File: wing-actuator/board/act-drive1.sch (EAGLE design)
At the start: 137 parts, among them J1 POWER_JACKPTH_LOCK, Q1 BSS123, Q2 BSS123, Q3 BSS123, Q4 BSS123, Q5 BSS123, Q6 BSS123, T1 ATB3225, U1 LT3468-1, X1 SMA-142-0701-801/806, X2 SMA-142-0701-801/806, X3 SMA-142-0701-801/806, X4 SMA-142-0701-801/806, X5 2516-, X6 2516-, X7 SSW-102-02-S-D

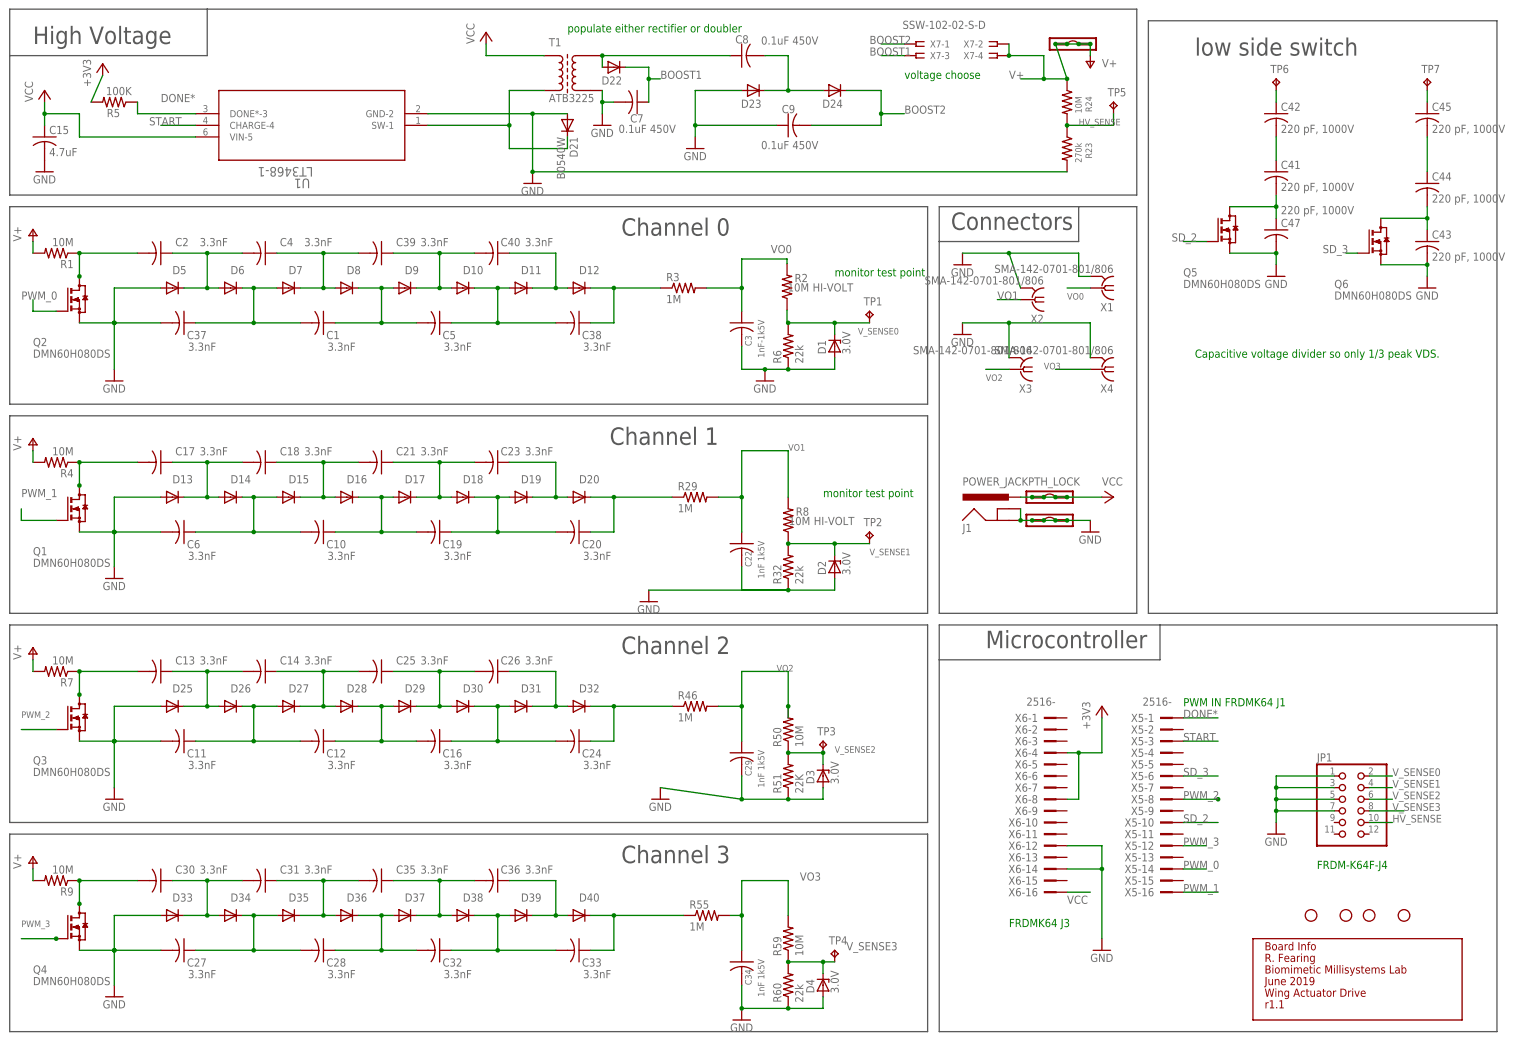
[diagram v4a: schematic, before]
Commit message: renumbered parts
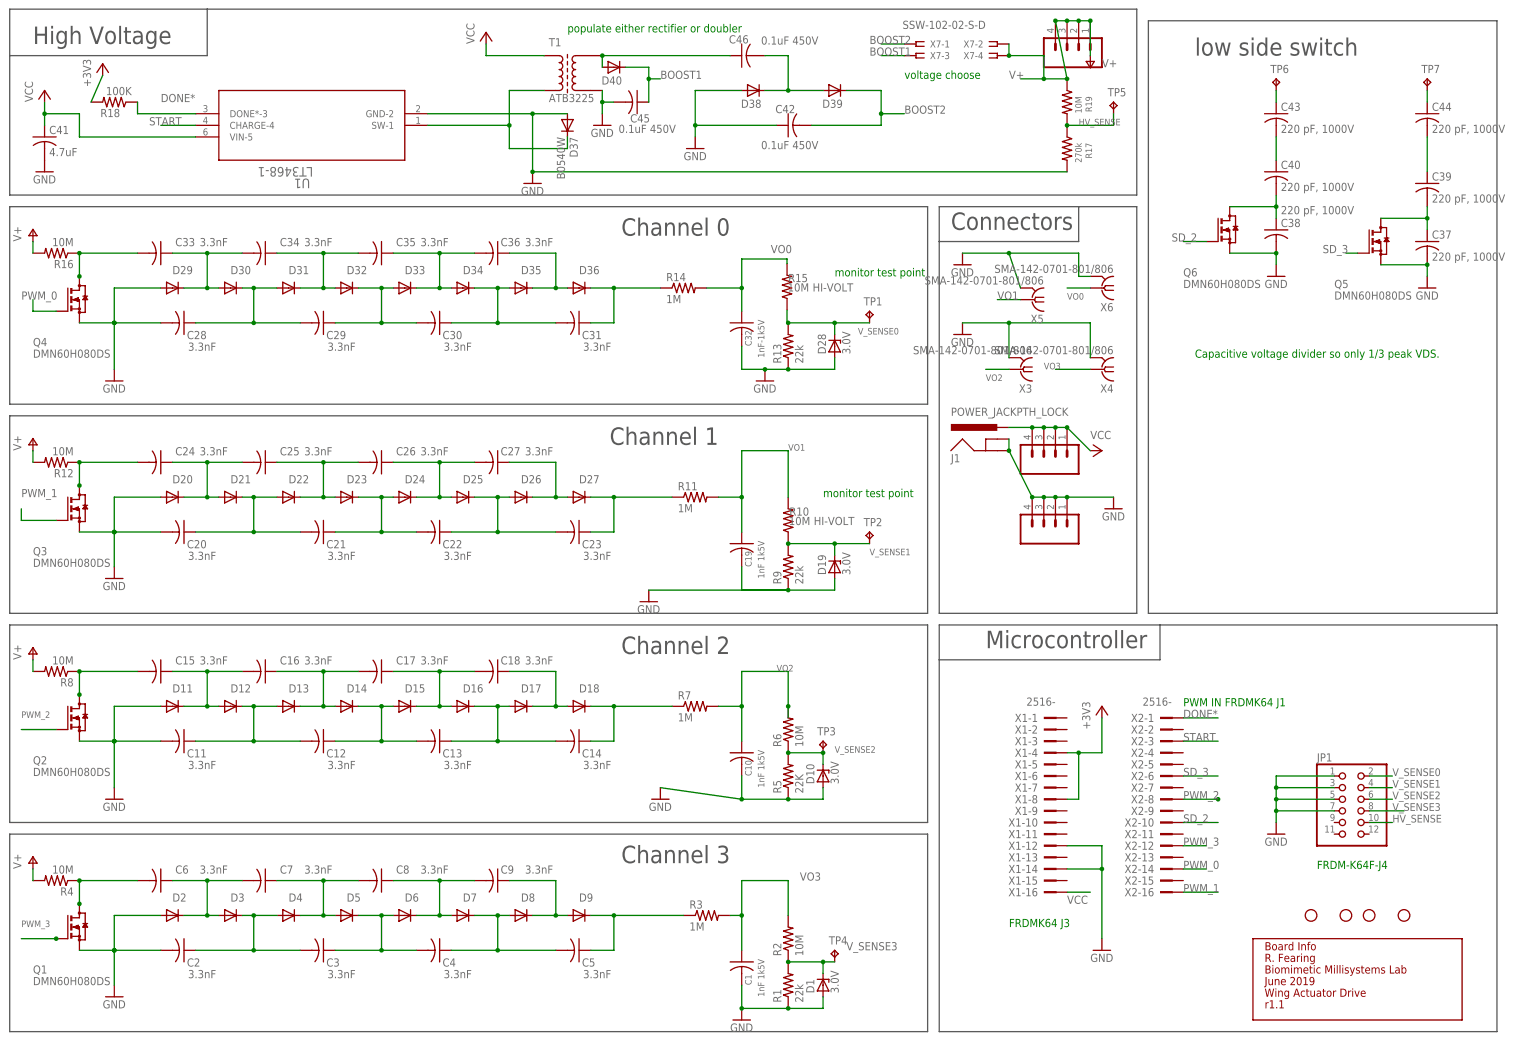
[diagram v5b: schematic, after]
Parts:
- removed C47: 220 pF, 1000V, rcl:C-USC1206
- removed R32, R60: 22k, rcl:R-US_R1206
- removed R46, R55: 1M, rcl:R-US_R1206
- removed R50, R59: 10M, rcl:R-US_R2010
- removed R51: 22K, rcl:R-US_R1206
- removed VCC: (no value), modular_robotics:M04LOCK
- added C46: 0.1uF 450V, rcl:C-USC1206
- added JP3: (no value), modular_robotics:M04LOCK
- added R10, R15: 10M, rcl:R-US_R2010
- added R12, R16: 10M, rcl:R-US_R1206
- added R13: 22k, rcl:R-US_R1206
- added R14: 1M, rcl:R-US_R1206
- added R18: 100K, resistor:R-US_R1206
- C1, C10, C19: value 3.3nF -> 1nF 1k5V; device rcl:C-USC0805K -> rcl:C-USC1206
- C15: value 4.7uF -> 3.3nF; device rcl:C-USC1206 -> rcl:C-USC0805K
- C22, C29, C34: value 1nF 1k5V -> 3.3nF; device rcl:C-USC1206 -> rcl:C-USC0805K
- C3: value 1nF-1k5V -> 3.3nF; device rcl:C-USC1206 -> rcl:C-USC0805K
- C32: value 3.3nF -> 1nF-1k5V; device rcl:C-USC0805K -> rcl:C-USC1206
- C37, C38, C39, C40: value 3.3nF -> 220 pF, 1000V; device rcl:C-USC0805K -> rcl:C-USC1206; DIGIKEY (none) -> 311-4469-1-ND
- C41: value 220 pF, 1000V -> 4.7uF; DIGIKEY 311-4469-1-ND -> (none)
- C42, C45: value 220 pF, 1000V -> 0.1uF 450V; DIGIKEY 311-4469-1-ND -> 445-7758-1-ND
- C7, C8, C9: value 0.1uF 450V -> 3.3nF; device rcl:C-USC1206 -> rcl:C-USC0805K; DIGIKEY 445-7758-1-ND -> (none)
- D10, D19, D28: value (none) -> 3.0V; device diode:DIODE-SOD323-W -> diode:ZENER-DIODESOD80C; PANASONIC DA2JF8100L -> (none)
- D18, D20, D24, D29: DIGIKEY (none) -> DA2JF8100LCT-ND
- D2, D3, D4: value 3.0V -> (none); device diode:ZENER-DIODESOD80C -> diode:DIODE-SOD323-W; PANASONIC (none) -> DA2JF8100L
- D21: value B0540W -> (none); device diode:DIODE-SOD123 -> diode:DIODE-SOD323-W; DIGIKEY (none) -> DA2JF8100LCT-ND; PANASONIC (none) -> DA2JF8100L
- D37: value (none) -> B0540W; device diode:DIODE-SOD323-W -> diode:DIODE-SOD123; PANASONIC DA2JF8100L -> (none)
- R1, R9: value 10M -> 22k
- R2: HI-VOLT 800 -> (none)
- R5: value 100K -> 22K; device resistor:R-US_R1206 -> rcl:R-US_R1206
- R6: value 22k -> 10M; device rcl:R-US_R1206 -> rcl:R-US_R2010
- R7: value 10M -> 1M
- R8: device rcl:R-US_R2010 -> rcl:R-US_R1206; HI-VOLT 2000 -> (none)
- T1: device lt3468-1:ATB3225 -> ActuatorDrive:ATB3225
- X1, X2: value SMA-142-0701-801/806 -> 2516-; device con-coax:SMA-142-0701-801/806 -> con-3m:2516-
- X5, X6: value 2516- -> SMA-142-0701-801/806; device con-3m:2516- -> con-coax:SMA-142-0701-801/806
- renumbered GND to JP2, H5 to H1, H6 to H2, H7 to H3, H8 to H4, HV_OUT to JP4, R23 to R17, R24 to R19, R29 to R11, U$18 to I1
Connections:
- net +3V3: now also R18.2, X1-4.KL, X1-8.KL; no longer R5.2, X6-4.KL, X6-8.KL
- net BOOST: now also C46.2, D38.C, D39.A; no longer C8.2, D23.C, D24.A
- net BOOST1: now also C45.1, D40.C; no longer C7.1, D22.C
- net BOOST2: now also C42.2, D39.C; no longer C9.2, D24.C
- net DONE*: now also R18.1, X2-1.KL; no longer R5.1, X5-1.KL
- net GND: now also C1.2, C10.2, C19.2, C2.2, C20.2, C28.2, C32.2, C38.2, C41.2, C42.1, C45.2, D10.A, D11.A, D19.A, D20.A, D28.A, D29.A, D37.A, D38.A, R1.1, R13.1, R5.1, R9.1, X1-12.KL, X1-14.KL, X5.2, X6.2; no longer C15.2, C22.2, C27.2, C29.2, C3.2, C34.2, C43.2, C47.2, C6.2, C7.2, C9.1, D13.A, D21.A, D23.A, D25.A, D3.A, D33.A, D4.A, D5.A, R32.1, R51.1, R6.1, R60.1, X1.2, X2.2, X6-12.KL, X6-14.KL
- net N$1: now also C29.1, C30.2, D32.C, D33.A; no longer C1.1, C5.2, D8.C, D9.A
- net N$10: now also C35.1, C36.2, D33.C, D34.A; no longer C39.1, C40.2, D10.A, D9.C
- net N$11: now also C24.1, C25.2, D20.C, D21.A; no longer C17.1, C18.2, D13.C, D14.A
- net N$12: now also D37.C; no longer D21.C
- net N$13: now also C20.1, C21.2, D21.C, D22.A; no longer C10.2, C6.1, D14.C, D15.A
- net N$14: now also C27.1, D26.C, D27.A; no longer C23.1, D19.C, D20.A
- net N$15: now also C21.1, C22.2, D23.C, D24.A; no longer C10.1, C19.2, D16.C, D17.A
- net N$16: now also C22.1, C23.2, D25.C, D26.A; no longer C19.1, C20.2, D18.C, D19.A
- net N$17: now also C15.1, C16.2, D11.C, D12.A; no longer C13.1, C14.2, D25.C, D26.A
- net N$18: now also D12.C, D13.A; no longer D26.C, D27.A
- net N$2: now also C33.1, C34.2, D29.C, D30.A; no longer C2.1, C4.2, D5.C, D6.A
- net N$20: now also C18.1, D17.C, D18.A; no longer C26.1, D31.C, D32.A
- net N$21: now also C25.1, C26.2, D22.C, D23.A; no longer C18.1, C21.2, D15.C, D16.A
- net N$22: now also C26.1, C27.2, D24.C, D25.A; no longer C21.1, C23.2, D17.C, D18.A
- net N$23: now also C24.2, Q3.D, R12.1; no longer C17.2, Q1.D, R4.1
- net N$24: now also C13.2, D14.C, D15.A; no longer C16.2, D28.C, D29.A
- net N$25: now also C13.1, C14.2, D16.C, D17.A; no longer C16.1, C24.2, D30.C, D31.A
- net N$26: now also C5.1, D9.C, R3.1; no longer C33.1, D40.C, R55.1
- net N$27: now also C16.1, C17.2, D13.C, D14.A; no longer C14.1, C25.2, D27.C, D28.A
- net N$29: now also C17.1, C18.2, D15.C, D16.A; no longer C25.1, C26.2, D29.C, D30.A
- net N$3: now also C31.1, D36.C, R14.1; no longer C38.1, D12.C, R3.1
- net N$30: now also C15.2, Q2.D, R8.1; no longer C13.2, Q3.D, R7.1
- net N$32: now also C6.1, C7.2, D2.C, D3.A; no longer C30.1, C31.2, D33.C, D34.A
- net N$33: now also C2.1, C3.2, D3.C, D4.A; no longer C27.1, C28.2, D34.C, D35.A
- net N$34: now also C9.1, D8.C, D9.A; no longer C36.1, D39.C, D40.A
- net N$35: now also C3.1, C4.2, D5.C, D6.A; no longer C28.1, C32.2, D36.C, D37.A
- net N$36: now also C4.1, C5.2, D7.C, D8.A; no longer C32.1, C33.2, D38.C, D39.A
- net N$37: now also C7.1, C8.2, D4.C, D5.A; no longer C31.1, C35.2, D35.C, D36.A
- net N$38: now also C8.1, C9.2, D6.C, D7.A; no longer C35.1, C36.2, D37.C, D38.A
- net N$39: now also C6.2, Q1.D, R4.1; no longer C30.2, Q4.D, R9.1
- net N$4: now also C14.1, D18.C, R7.1; no longer C24.1, D32.C, R46.1
- net N$40: now also C43.1; no longer C42.1
- net N$41: now also C40.1, C43.2; no longer C41.1, C42.2
- net N$42: now also C38.1, C40.2, Q6.D; no longer C41.2, C47.1, Q5.D
- net N$43: now also C44.1; no longer C45.1
- net N$44: now also C39.1, C44.2; no longer C44.1, C45.2
- net N$45: now also C37.1, C39.2, Q5.D; no longer C43.1, C44.2, Q6.D
- net N$5: now also C28.1, C29.2, D30.C, D31.A; no longer C1.2, C37.1, D6.C, D7.A
- net N$59: now also C36.1, D35.C, D36.A; no longer C40.1, D11.C, D12.A
- net N$6: now also C46.1, D40.A; no longer C8.1, D22.A
- net N$61: now also C30.1, C31.2, D34.C, D35.A; no longer C38.2, C5.1, D10.C, D11.A
- net N$7: now also C34.1, C35.2, D31.C, D32.A; no longer C39.2, C4.1, D7.C, D8.A
- net N$8: now also C33.2, Q4.D, R16.1; no longer C2.2, Q2.D, R1.1
- net N$9: now also C23.1, D27.C; no longer C20.1, D20.C
- net PWM_0: now also Q4.G, X2-14.KL; no longer Q2.G, X5-14.KL
- net PWM_1: now also Q3.G, X2-16.KL; no longer Q1.G, X5-16.KL
- net PWM_2: now also Q2.G, X2-8.KL; no longer Q3.G, X5-8.KL
- net PWM_3: now also Q1.G, X2-12.KL; no longer Q4.G, X5-12.KL
- net SD_2: now also Q6.G, X2-10.KL; no longer Q5.G, X5-10.KL
- net SD_3: now also Q5.G, X2-6.KL; no longer Q6.G, X5-6.KL
- net START: now also X2-3.KL; no longer X5-3.KL
- net V+: now also R12.2, R16.2, R8.2; no longer R1.2, R7.2, R9.2
- net VCC: now also C41.1, JP3.1, JP3.2, JP3.3, JP3.4, X1-16.KL; no longer C15.1, VCC.1, VCC.2, VCC.3, VCC.4, X6-16.KL
- net VO0: now also C32.1, R14.2, R15.2, X6.1; no longer C3.1, R2.2, R3.2, X1.1
- net VO1: now also C19.1, R10.2, X5.1; no longer C22.1, R8.2, X2.1
- net VO2: now also C10.1, R6.2, R7.2; no longer C29.1, R46.2, R50.2
- net VO3: now also C1.1, R2.2, R3.2; no longer C34.1, R55.2, R59.2
- net V_SENSE0: now also D28.C, R13.2, R15.1; no longer D1.C, R2.1, R6.2
- net V_SENSE1: now also D19.C, R10.1, R9.2; no longer D2.C, R32.2, R8.1
- net V_SENSE2: now also D10.C, R5.2, R6.1; no longer D3.C, R50.1, R51.2
- net V_SENSE3: now also D1.C, R1.2, R2.1; no longer D4.C, R59.1, R60.2
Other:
- moved on the sheet: C1, C10, C13, C14, C15, C16, C17, C18, C19, C2, C20, C21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

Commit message: added digikey part #s
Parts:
- removed X1, X2: 2516-, con-3m:2516-
- added D41: 3.0V, diode:ZENER-DIODESOD80C
- added SV1, SV2: (no value), con-harting-ml:ML16
- C1, C10, C19: DIGIKEY (none) -> 399-7078-1-ND
- C32: value 1nF-1k5V -> 1nF 1k5V; DIGIKEY (none) -> 399-7078-1-ND
- C33: DIGIKEY (none) -> 399-5576-1-ND
- C41: DIGIKEY (none) -> 399-1265-1-ND
- D28: DIGIKEY (none) -> MM3Z3V0ST1GOSCT-ND
- D37: DIGIKEY (none) -> B0540W-FDICT-ND
- J1: DIGIKEY (none) -> CP-202A-ND
- Q4: DIGIKEY (none) -> DMN60H080DS-7DICT-ND; MOUSER (none) -> 621-DMN60H080DS-7; PART# DMN60H080DS -> (none)
- Q5, Q6: DIGIKEY (none) -> DMN60H080DS-7DICT-ND
- R10: DIGIKEY (none) -> CHV2010-FX-1005ELFCT-ND
- R11, R14, R3, R7: value 1M -> 1.0M; DIGIKEY (none) -> P1.0MECT-ND
- R12, R16, R4, R8: value 10M -> 1.0M; DIGIKEY (none) -> P1.0MECT-ND
- R13: DIGIKEY (none) -> P22KECT-ND
- R15: DIGIKEY (none) -> CHV2010-FX-1005ELFCT-ND; HI-VOLT 800 -> 2000
- R17: DIGIKEY (none) -> P270KECT-ND
- R18: value 100K -> 22K
- R19: DIGIKEY (none) -> P10MECT-ND
- R2, R6: DIGIKEY (none) -> CHV2010-FX-1005ELFCT-ND; HI-VOLT (none) -> 2000
- T1: DIGIKEY (none) -> 445-8636-1-ND
- U1: DIGIKEY (none) -> LT3468ES5#TRMPBFCT-ND
- X5: DIGIKEY (none) -> J502-ND
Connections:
- net +3V3: now also SV1.4, SV1.8; no longer X1-4.KL, X1-8.KL
- net DONE*: now also SV2.1; no longer X2-1.KL
- net GND: now also D41.A, SV1.12, SV1.14; no longer X1-12.KL, X1-14.KL
- net HV_SENSE: now also D41.C
- net PWM_0: now also SV2.14; no longer X2-14.KL
- net PWM_1: now also SV2.16; no longer X2-16.KL
- net PWM_2: now also SV2.8; no longer X2-8.KL
- net PWM_3: now also SV2.12; no longer X2-12.KL
- net SD_2: now also SV2.10; no longer X2-10.KL
- net SD_3: now also SV2.6; no longer X2-6.KL
- net START: now also SV2.3; no longer X2-3.KL
- net VCC: now also SV1.16; no longer X1-16.KL
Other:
- moved on the sheet: JP1

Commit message: changed all lines to 8 mil min width
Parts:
- C1, C10, C19, C32: value 1nF 1k5V -> 1nF
- C37, C38, C39, C40, C43, C44: value 220 pF, 1000V -> 220 pF
- C42, C45, C46: value 0.1uF 450V -> 0.1uF
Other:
- note added: "1.5kv cap"
- note added: "these caps 450 Vmin"
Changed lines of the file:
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@@
 <attribute name="DIGIKEY" value="P1.0MECT-ND"/>
 </part>
-<part name="C32" library="rcl" deviceset="C-US" device="C1206" value="1nF 1k5V">
-<attribute name="DIGIKEY" value="399-7078-1-ND
-"/>
+<part name="C32" library="rcl" deviceset="C-US" device="C1206" value="1nF">
+<attribute name="DIGIKEY" value="399-7078-1-ND "/>
 </part>
 <part name="R13" library="rcl" deviceset="R-US_" device="R1206" value="22k">
@@
 </part>
 <part name="R19" library="rcl" deviceset="R-US_" device="R1206" value="10M">
-<attribute name="DIGIKEY" value="P10MECT-ND
-"/>
+<attribute name="DIGIKEY" value="P10MECT-ND "/>
 </part>
 <part name="P+7" library="supply1" deviceset="V+" device=""/>
 <part name="JP4" library="modular_robotics" deviceset="M04" device="LOCK"/>
 <part name="J1" library="SparkFun-Connectors" deviceset="POWER_JACK" device="PTH_LOCK">
-<attribute name="DIGIKEY" value="CP-202A-ND
-"/>
+<attribute name="DIGIKEY" value="CP-202A-ND "/>
 <attribute name="DIMENSIONS" value="5.5mm-diam"/>
 </part>
@@
 <attribute name="DIGIKEY" value="P1.0MECT-ND"/>
 </part>
-<part name="C19" library="rcl" deviceset="C-US" device="C1206" value="1nF 1k5V">
+<part name="C19" library="rcl" deviceset="C-US" device="C1206" value="1nF">
 <attribute name="DIGIKEY" value="399-7078-1-ND"/>
 </part>
@@
 <attribute name="DIGIKEY" value="P1.0MECT-ND"/>
 </part>
-<part name="C10" library="rcl" deviceset="C-US" device="C1206" value="1nF 1k5V">
+<part name="C10" library="rcl" deviceset="C-US" device="C1206" value="1nF">
 <attribute name="DIGIKEY" value="399-7078-1-ND"/>
 </part>
@@
 <attribute name="DIGIKEY" value="P1.0MECT-ND"/>
 </part>
-<part name="C1" library="rcl" deviceset="C-US" device="C1206" value="1nF 1k5V">
+<part name="C1" library="rcl" deviceset="C-US" device="C1206" value="1nF">
 <attribute name="DIGIKEY" value="399-7078-1-ND"/>
 </part>
@@
 <attribute name="PANASONIC" value="DA2JF8100L"/>
 </part>
-<part name="C45" library="rcl" library_urn="urn:adsk.eagle:library:334" deviceset="C-US" device="C1206" package3d_urn="urn:adsk.eagle:package:23618/2" value="0.1uF 450V">
+<part name="C45" library="rcl" library_urn="urn:adsk.eagle:library:334" deviceset="C-US" device="C1206" package3d_urn="urn:adsk.eagle:package:23618/2" value="0.1uF">
 <spice>
 <pinmapping spiceprefix="C">
@@
 </part>
 <part name="GND19" library="supply1" library_urn="urn:adsk.eagle:library:371" deviceset="GND" device=""/>
-<part name="C46" library="rcl" library_urn="urn:adsk.eagle:library:334" deviceset="C-US" device="C1206" package3d_urn="urn:adsk.eagle:package:23618/2" value="0.1uF 450V">
+<part name="C46" library="rcl" library_urn="urn:adsk.eagle:library:334" deviceset="C-US" device="C1206" package3d_urn="urn:adsk.eagle:package:23618/2" value="0.1uF">
 <spice>
 <pinmapping spiceprefix="C">
@@
 <attribute name="DIGIKEY" value="445-7758-1-ND "/>
 </part>
-<part name="C42" library="rcl" library_urn="urn:adsk.eagle:library:334" deviceset="C-US" device="C1206" package3d_urn="urn:adsk.eagle:package:23618/2" value="0.1uF 450V">
+<part name="C42" library="rcl" library_urn="urn:adsk.eagle:library:334" deviceset="C-US" device="C1206" package3d_urn="urn:adsk.eagle:package:23618/2" value="0.1uF">
 <spice>
 <pinmapping spiceprefix="C">
@@
 </part>
 <part name="U1" library="ActuatorDrive" deviceset="LT3468-1" device="">
-<attribute name="DIGIKEY" value=" 	LT3468ES5#TRMPBFCT-ND "/>
+<attribute name="DIGIKEY" value="  LT3468ES5#TRMPBFCT-ND "/>
 </part>
 <part name="Q6" library="transistor-small-signal" library_urn="urn:adsk.eagle:library:401" deviceset="BSS123" device="">
@@
 <part name="GND13" library="supply1" deviceset="GND" device=""/>
 <part name="X7" library="con-samtec" library_urn="urn:adsk.eagle:library:184" deviceset="SSW-102-02-S-D" device=""/>
-<part name="C38" library="rcl" library_urn="urn:adsk.eagle:library:334" deviceset="C-US" device="C1206" package3d_urn="urn:adsk.eagle:package:23618/2" value="220 pF, 1000V">
+<part name="C38" library="rcl" library_urn="urn:adsk.eagle:library:334" deviceset="C-US" device="C1206" package3d_urn="urn:adsk.eagle:package:23618/2" value="220 pF">
 <spice>
 <pinmapping spiceprefix="C">
@@
 <attribute name="DIGIKEY" value="311-4469-1-ND "/>
 </part>
-<part name="C40" library="rcl" library_urn="urn:adsk.eagle:library:334" deviceset="C-US" device="C1206" package3d_urn="urn:adsk.eagle:package:23618/2" value="220 pF, 1000V">
+<part name="C40" library="rcl" library_urn="urn:adsk.eagle:library:334" deviceset="C-US" device="C1206" package3d_urn="urn:adsk.eagle:package:23618/2" value="220 pF">
 <spice>
 <pinmapping spiceprefix="C">
@@
 <attribute name="DIGIKEY" value="311-4469-1-ND "/>
 </part>
-<part name="C43" library="rcl" library_urn="urn:adsk.eagle:library:334" deviceset="C-US" device="C1206" package3d_urn="urn:adsk.eagle:package:23618/2" value="220 pF, 1000V">
+<part name="C43" library="rcl" library_urn="urn:adsk.eagle:library:334" deviceset="C-US" device="C1206" package3d_urn="urn:adsk.eagle:package:23618/2" value="220 pF">
 <spice>
 <pinmapping spiceprefix="C">
@@
 <attribute name="DIGIKEY" value="311-4469-1-ND "/>
 </part>
-<part name="C37" library="rcl" library_urn="urn:adsk.eagle:library:334" deviceset="C-US" device="C1206" package3d_urn="urn:adsk.eagle:package:23618/2" value="220 pF, 1000V">
+<part name="C37" library="rcl" library_urn="urn:adsk.eagle:library:334" deviceset="C-US" device="C1206" package3d_urn="urn:adsk.eagle:package:23618/2" value="220 pF">
 <spice>
 <pinmapping spiceprefix="C">
@@
 <attribute name="DIGIKEY" value="311-4469-1-ND "/>
 </part>
-<part name="C39" library="rcl" library_urn="urn:adsk.eagle:library:334" deviceset="C-US" device="C1206" package3d_urn="urn:adsk.eagle:package:23618/2" value="220 pF, 1000V">
+<part name="C39" library="rcl" library_urn="urn:adsk.eagle:library:334" deviceset="C-US" device="C1206" package3d_urn="urn:adsk.eagle:package:23618/2" value="220 pF">
 <spice>
 <pinmapping spiceprefix="C">
@@
 <attribute name="DIGIKEY" value="311-4469-1-ND "/>
 </part>
-<part name="C44" library="rcl" library_urn="urn:adsk.eagle:library:334" deviceset="C-US" device="C1206" package3d_urn="urn:adsk.eagle:package:23618/2" value="220 pF, 1000V">
+<part name="C44" library="rcl" library_urn="urn:adsk.eagle:library:334" deviceset="C-US" device="C1206" package3d_urn="urn:adsk.eagle:package:23618/2" value="220 pF">
 <spice>
 <pinmapping spiceprefix="C">
@@
 <text x="284.48" y="96.52" size="1.778" layer="91">Capacitive voltage divider so only 1/3 peak VDS.</text>
 <text x="220.98" y="157.48" size="1.778" layer="91">voltage choose</text>
+<text x="208.28" y="142.24" size="1.778" layer="91">these caps 450 Vmin</text>
+<text x="170.18" y="101.6" size="1.778" layer="91">1.5kv cap</text>
+<text x="170.18" y="53.34" size="1.778" layer="91">1.5kv cap</text>
+<text x="170.18" y="10.16" size="1.778" layer="91">1.5kv cap</text>
+<text x="170.18" y="-38.1" size="1.778" layer="91">1.5kv cap</text>
 </plain>
 <instances>
@@
 </instance>
 <instance part="X6" gate="G1" x="264.16" y="111.76" smashed="yes" rot="R180">
-<attribute name="VALUE" x="266.7" y="116.84" size="1.778" layer="96" rot="R180"/>
 <attribute name="NAME" x="266.7" y="108.458" size="1.778" layer="95" rot="R180"/>
 </instance>
 <instance part="X5" gate="G1" x="248.92" y="109.22" smashed="yes" rot="R180">
-<attribute name="VALUE" x="251.46" y="114.3" size="1.778" layer="96" rot="R180"/>
 <attribute name="NAME" x="251.46" y="105.918" size="1.778" layer="95" rot="R180"/>
 <attribute name="DIGIKEY" x="248.92" y="109.22" size="1.778" layer="96" rot="R180" display="off"/>
 </instance>
 <instance part="X3" gate="G1" x="246.38" y="93.98" smashed="yes" rot="R180">
-<attribute name="VALUE" x="248.92" y="99.06" size="1.778" layer="96" rot="R180"/>
 <attribute name="NAME" x="248.92" y="90.678" size="1.778" layer="95" rot="R180"/>
 </instance>
 <instance part="X4" gate="G1" x="264.16" y="93.98" smashed="yes" rot="R180">
-<attribute name="VALUE" x="266.7" y="99.06" size="1.778" layer="96" rot="R180"/>
 <attribute name="NAME" x="266.7" y="90.678" size="1.778" layer="95" rot="R180"/>
 </instance>
